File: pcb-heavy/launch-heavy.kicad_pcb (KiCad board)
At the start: 2 copper layers, 76 x 112 mm, 73 parts, among them J7 AFC07-S20FCC-00

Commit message: rename launch-tenkey to launch-heavy
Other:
- board text added: "Launch Heavy Rev 0.0 Board must be RoHS compliant Fabricate to IPC-A-600 Class II Material: FR4 Outer copper, min 33.4 um finished Black LPI solder mask over bare copper Vendor may remove solder mask from via holes, maximum of drill size + 3 mil Finish: OSP Silkscreen: white non conductive 100% electrical test required Remove all unused pads from inner layers All layers positive Overall thickness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"
- board text added: "launch_heavy 0.0"
- board text removed: "Launch Tenkey Rev 0.0 Board must be RoHS compliant Fabricate to IPC-A-600 Class II Material: FR4 Outer copper, min 33.4 um finished Black LPI solder mask over bare copper Vendor may remove solder mask from via holes, maximum of drill size + 3 mil Finish: OSP Silkscreen: white non conductive 100% electrical test required Remove all unused pads from inner layers All layers positive Overall thicknes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"
- board text removed: "launch_tenkey 0.0"

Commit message: set versions
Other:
- board text added: "Launch Heavy Rev 1.0 Board must be RoHS compliant Fabricate to IPC-A-600 Class II Material: FR4 Outer copper, min 33.4 um finished Black LPI solder mask over bare copper Vendor may remove solder mask from via holes, maximum of drill size + 3 mil Finish: OSP Silkscreen: white non conductive 100% electrical test required Remove all unused pads from inner layers All layers positive Overall thickness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"
- board text added: "launch_heavy 1.0"
- board text removed: "Launch Heavy Rev 0.0 Board must be RoHS compliant Fabricate to IPC-A-600 Class II Material: FR4 Outer copper, min 33.4 um finished Black LPI solder mask over bare copper Vendor may remove solder mask from via holes, maximum of drill size + 3 mil Finish: OSP Silkscreen: white non conductive 100% electrical test required Remove all unused pads from inner layers All layers positive Overall thickness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"
- board text removed: "launch_heavy 0.0"
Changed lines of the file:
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@@
     (effects (font (size 1 1) (thickness 0.15)) (justify left))
   )
-  (gr_text "launch_heavy 0.0" (at 71 60) (layer "B.SilkS")
+  (gr_text "launch_heavy 1.0" (at 71 60) (layer "B.SilkS")
     (effects (font (size 1.5 1.5) (thickness 0.3)) (justify mirror))
   )
@@
     (effects (font (size 1 1) (thickness 0.15)) (justify left))
   )
-  (gr_text "Launch Heavy Rev 0.0\nBoard must be RoHS compliant\nFabricate to IPC-A-600 Class II\nMaterial: FR4\nOuter copper, min 33.4 um finished\nBlack LPI solder mask over bare copper\nVendor may remove solder mask from via holes, \n     maximum of drill size + 3 mil\nFinish: OSP\nSilkscreen: white non conductive\n100% electrical test required\nRemove all unused pads from inner layers\nAll layers positive\nOverall thickness: 1.6 mm +- 10 %\n" (at 102 48) (layer "Cmts.User")
+  (gr_text "Launch Heavy Rev 1.0\nBoard must be RoHS compliant\nFabricate to IPC-A-600 Class II\nMaterial: FR4\nOuter copper, min 33.4 um finished\nBlack LPI solder mask over bare copper\nVendor may remove solder mask from via holes, \n     maximum of drill size + 3 mil\nFinish: OSP\nSilkscreen: white non conductive\n100% electrical test required\nRemove all unused pads from inner layers\nAll layers positive\nOverall thickness: 1.6 mm +- 10 %\n" (at 102 48) (layer "Cmts.User")
     (effects (font (size 1 1) (thickness 0.15)) (justify left))
   )

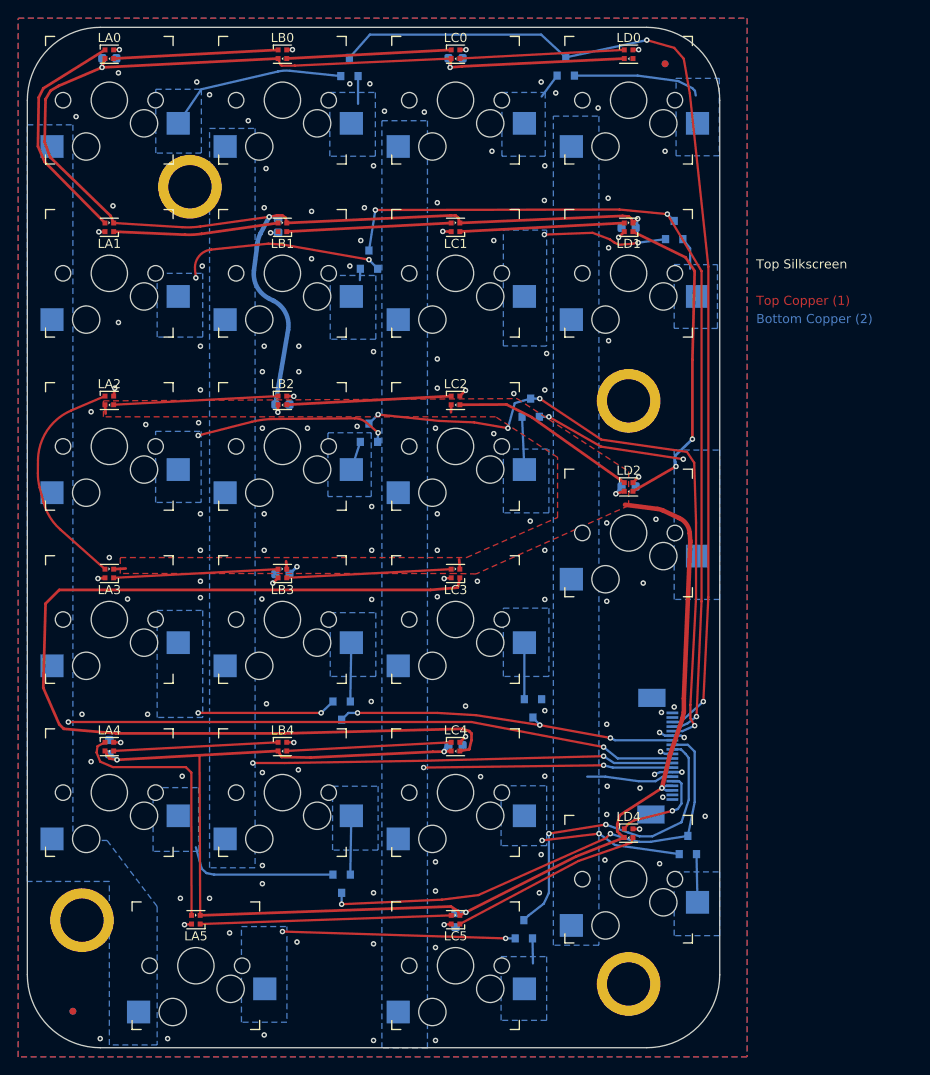
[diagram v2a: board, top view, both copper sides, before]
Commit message: launch heavy 1.1 move mounting holes to allow room for stabilizers no schematic changes round switch pads for improved clearance relocate D14 for mounting hole clearance
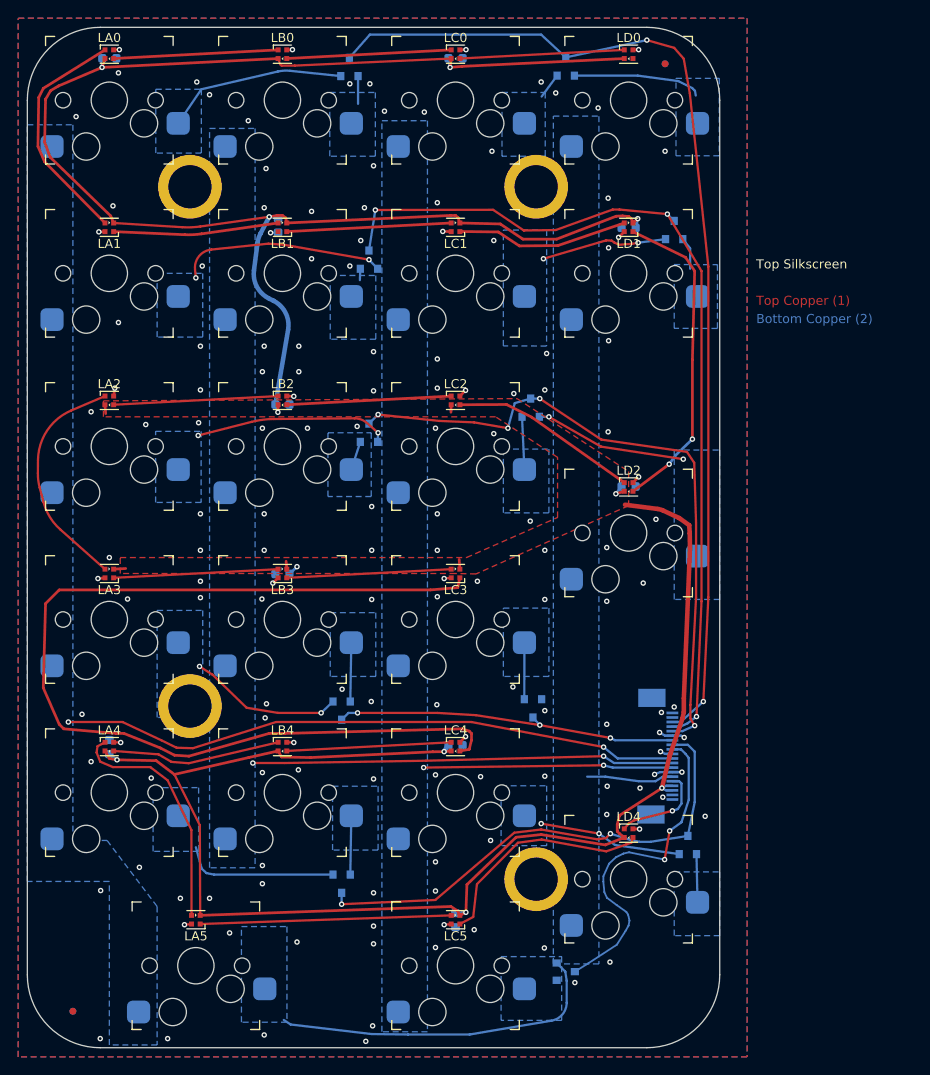
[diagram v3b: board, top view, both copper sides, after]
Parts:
- moved H2 26.3 mm to (39.9, 111.5)
- moved H5 25.6 mm to (77.8, 54.5)
- moved H3 15.3 mm to (77.8, 130.5)
- moved LOGO1 13.2 mm to (57.9, 55.6)
- moved D14 6.54 mm to (81.1, 140.7), turned to 0 degrees
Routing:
- net Net-(D14-Pad2): track 25.6 -> 37.2 mm, vias 2 -> 0
- net +3V6: track 335.4 -> 339.2 mm
- net Net-(LC5-Pad1): track 21.5 -> 25.0 mm
- net Net-(D14-Pad1): track 2.75 -> 0.00 mm
- net Net-(LA4-Pad1): track 28.8 -> 26.1 mm
- net Net-(D12-Pad1): track 15.3 -> 16.9 mm
- net /ROW11: track 35.3 -> 36.9 mm
- net /ROW10: track 53.1 -> 54.6 mm
- net /ROW7: track 96.8 -> 97.9 mm
- net /COLM: track 67.0 -> 68.1 mm
- net Net-(LC3-Pad1): track 109.0 -> 109.9 mm
- net Net-(LC1-Pad1): track 18.1 -> 18.9 mm
- net Net-(LD1-Pad1): track 36.0 -> 35.4 mm
- net GND: vias 141 -> 149
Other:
- board text added: "Launch Heavy Rev 1.1 Board must be RoHS compliant Fabricate to IPC-A-600 Class II Material: FR4 Outer copper, min 33.4 um finished Black LPI solder mask over bare copper Vendor may remove solder mask from via holes, maximum of drill size + 3 mil Finish: OSP Silkscreen: white non conductive 100% electrical test required Remove all unused pads from inner layers All layers positive Overall thickness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"
- board text added: "launch_heavy 1.1"
- board text removed: "Launch Heavy Rev 1.0 Board must be RoHS compliant Fabricate to IPC-A-600 Class II Material: FR4 Outer copper, min 33.4 um finished Black LPI solder mask over bare copper Vendor may remove solder mask from via holes, maximum of drill size + 3 mil Finish: OSP Silkscreen: white non conductive 100% electrical test required Remove all unused pads from inner layers All layers positive Overall thickness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"
- board text removed: "launch_heavy 1.0"

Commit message: rotate +, enter on heavy, move hole
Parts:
- moved H3 19.0 mm to (58.9, 130.5)
- moved D49 17.3 mm to (77.7, 130.6), turned to -90 degrees
- moved C3 7.21 mm to (93.1, 92.5)
- moved LD2 7.18 mm to (93.1, 92.5)
- moved LD4 7.18 mm to (93.1, 130.5)
- moved D13 5.59 mm to (51.0, 132.0)
- turned SWD2 to 90 degrees
- turned SWD4 to 90 degrees
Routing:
- net +3V6: track 339.2 -> 311.1 mm, vias 11 -> 12
- net /ROW11: track 36.9 -> 51.5 mm, vias 2 -> 0
- net Net-(D49-Pad2): track 15.7 -> 3.00 mm, vias 2 -> 0
- net Net-(D47-Pad1): track 16.8 -> 26.6 mm
- net Net-(LC2-Pad3): track 20.7 -> 28.6 mm
- net Net-(D13-Pad1): track 17.1 -> 11.8 mm
- net Net-(D49-Pad1): track 5.29 -> 8.93 mm
- net /ROW8: track 72.1 -> 69.1 mm
- net /ROW10: track 54.6 -> 57.4 mm, vias 2 -> 5
- net Net-(LD1-Pad1): track 35.4 -> 38.2 mm
- net Net-(LC5-Pad1): track 25.0 -> 27.6 mm
- net /LEDI: track 10.4 -> 11.7 mm
- net Net-(D13-Pad2): track 6.46 -> 5.52 mm
- net GND: track 23.6 -> 24.5 mm, vias 149 -> 154
- net /COLD: track 9.55 -> 8.92 mm
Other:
- board text added: "Launch Heavy Rev 1.2 Board must be RoHS compliant Fabricate to IPC-A-600 Class II Material: FR4 Outer copper, min 33.4 um finished Black LPI solder mask over bare copper Vendor may remove solder mask from via holes, maximum of drill size + 3 mil Finish: OSP Silkscreen: white non conductive 100% electrical test required Remove all unused pads from inner layers All layers positive Overall thickness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"
- board text added: "launch_heavy 1.2"
- board text removed: "Launch Heavy Rev 1.1 Board must be RoHS compliant Fabricate to IPC-A-600 Class II Material: FR4 Outer copper, min 33.4 um finished Black LPI solder mask over bare copper Vendor may remove solder mask from via holes, maximum of drill size + 3 mil Finish: OSP Silkscreen: white non conductive 100% electrical test required Remove all unused pads from inner layers All layers positive Overall thickness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"
- board text removed: "launch_heavy 1.1"
